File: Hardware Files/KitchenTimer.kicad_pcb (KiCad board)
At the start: 2 copper layers, 100 x 100 mm, 89 parts, among them J1 Conn_01x04, J2 USB_B_Micro, J3 Battery, Q1 P 1V 250uA 4A SOT-23, Q10 Q_NMOS_GSD, Q11 Q_NMOS_GSD, Q12 Q_NMOS_GSD, Q13 Q_NMOS_GSD, Q14 -30V 12A 14mΩ @ 8A, Q15 20V 7.5A 24mΩ @ 2.5Vgs, Q2 P 1V 250uA 4A SOT-23, Q3 P 1V 250uA 4A SOT-23, Q4 P 1V 250uA 4A SOT-23, Q5 P 1V 250uA 4A SOT-23, Q6 Q_NMOS_GSD, Q7 Q_NMOS_GSD, Q8 Q_NMOS_GSD, Q9 Q_NMOS_GSD, SW1 SW_SPST, SW2 SW_SPST, SW3 SW_Push_Dual, SW4 SW_Push_Dual, SW5 SW_Push_Dual, SW6 SW_Push_Dual, U1 74HC595, U2 74HC595, U3 ESP-WROOM-02D, U4 AP34063S8G-13, U5 TP4056, U6 AP9101CK6, U7 NCP1117ST50T3G, U8 NCP1117ST33T3G

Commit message: update layout
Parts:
- added C1: 1uF, Capacitor_SMD:C_1206_3216Metric_Pad1.33x1.80mm_HandSolder, B.Cu at (162.0, -12.0)
- added C10: 1uF, Capacitor_SMD:C_1206_3216Metric_Pad1.33x1.80mm_HandSolder, B.Cu at (152.4, -15.3)
- added C2: 1uF, Capacitor_SMD:C_1206_3216Metric_Pad1.33x1.80mm_HandSolder, B.Cu at (162.0, -15.3)
- added C3: 1uF, Capacitor_SMD:C_1206_3216Metric_Pad1.33x1.80mm_HandSolder, B.Cu at (40.0, -21.5)
- added C4: 10uF, Capacitor_SMD:C_1206_3216Metric_Pad1.33x1.80mm_HandSolder, B.Cu at (42.5, -21.5)
- added C5: 1uF, Capacitor_SMD:C_1206_3216Metric_Pad1.33x1.80mm_HandSolder, B.Cu at (146.4, -12.0)
- added C6: 1uF, Capacitor_SMD:C_1206_3216Metric_Pad1.33x1.80mm_HandSolder, B.Cu at (140.4, -18.7)
- added C7: 1uF, Capacitor_SMD:C_1206_3216Metric_Pad1.33x1.80mm_HandSolder, B.Cu at (146.4, -15.3)
- added C8: 1uF, Capacitor_SMD:C_1206_3216Metric_Pad1.33x1.80mm_HandSolder, B.Cu at (152.4, -12.0)
- added C9: 1uF, Capacitor_SMD:C_1206_3216Metric_Pad1.33x1.80mm_HandSolder, B.Cu at (146.4, -18.7)
- moved R23 190.7 mm to (28.0, 46.0), turned to 90 degrees
- moved R24 190.4 mm to (28.0, 54.0), turned to 90 degrees
- moved Q11 187.7 mm to (31.0, 50.0), turned to 0 degrees
- moved Q6 184.7 mm to (31.0, 46.0), turned to 0 degrees
- moved Q7 184.5 mm to (31.0, 54.0), turned to 0 degrees
- moved R27 176.0 mm to (42.5, 69.0), turned to 180 degrees
- moved U3 174.1 mm to (37.0, -19.5)
- moved Q10 173.2 mm to (42.5, 66.0), turned to 90 degrees
- moved R26 171.7 mm to (46.5, 69.0), turned to 180 degrees
- moved Q9 168.9 mm to (46.5, 66.0), turned to 90 degrees
- moved Q13 167.4 mm to (50.5, 66.0), turned to 90 degrees
- moved R25 163.5 mm to (54.5, 69.0), turned to 180 degrees
- moved Q8 160.6 mm to (54.5, 66.0), turned to 90 degrees
- moved Q12 158.6 mm to (58.5, 66.0), turned to 90 degrees
- moved R18 154.4 mm to (40.0, 35.0), turned to 180 degrees
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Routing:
- net Net-(LED1-Pad9): track 0.00 -> 25.3 mm
- net Net-(LED1-Pad12): track 0.00 -> 15.6 mm
- net Net-(LED1-Pad13): track 0.00 -> 11.7 mm
- net LED_G_Sink: track 0.00 -> 6.83 mm
- net LED_C_Sink: track 0.00 -> 6.50 mm
- net LED_DP_Sink: track 0.00 -> 5.00 mm
- net LED_B_Sink: track 0.00 -> 4.71 mm
- net LED_D_Sink: track 0.00 -> 3.50 mm
- net Net-(LED1-Pad1): track 0.00 -> 3.43 mm
- net Net-(LED1-Pad2): track 0.00 -> 3.41 mm
- net Net-(LED1-Pad5): track 0.00 -> 3.40 mm
- net Net-(LED1-Pad3): track 0.00 -> 3.40 mm
- net Net-(LED1-Pad4): track 0.00 -> 3.38 mm
- net LED_F_Sink: track 0.00 -> 3.21 mm
- net Char_3: track 0.00 -> 2.05 mm
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
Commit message: reorganize mosfets
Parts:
- removed Q5: P 1V 250uA 4A SOT-23, Package_TO_SOT_SMD:SOT-23
- removed R22: 10k, Resistor_SMD:R_0805_2012Metric_Pad1.20x1.40mm_HandSolder
- moved C2 173.1 mm to (-7.00, 22.0), turned to 90 degrees
- moved C1 157.7 mm to (8.00, 22.0), turned to 90 degrees
- moved R14 130.1 mm to (-72.0, 32.0)
- moved R15 130.1 mm to (-56.0, 31.5)
- moved R29 87.1 mm to (-24.0, 41.0), turned to 0 degrees
- moved Q12 85.1 mm to (-24.0, 45.0), turned to 270 degrees
- moved R12 77.4 mm to (-24.0, 50.0), turned to 90 degrees
- moved R30 75.6 mm to (-24.0, 56.0), turned to 0 degrees
- moved Q13 74.7 mm to (-24.0, 60.0), turned to 270 degrees
- moved R13 71.6 mm to (-24.0, 65.0), turned to 90 degrees
- moved R26 67.6 mm to (-15.0, 41.0), turned to 0 degrees
- moved Q9 65.0 mm to (-15.0, 45.0), turned to 270 degrees
- moved Q8 62.2 mm to (-7.00, 75.0), turned to 270 degrees
- moved R25 61.5 mm to (-7.00, 71.0), turned to 0 degrees
- moved R21 61.4 mm to (-1.00, 41.0), turned to 180 degrees
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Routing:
- net LED_C: track 0.00 -> 61.6 mm
- net LED_F: track 0.00 -> 58.4 mm
- net Char_1: track 2.05 -> 57.1 mm
- net LED_E: track 0.00 -> 49.3 mm
- net LED_B: track 0.00 -> 45.5 mm
- net LED_DP: track 0.00 -> 44.8 mm
- net Char_2: track 2.05 -> 40.6 mm
- net LED_D: track 0.00 -> 36.7 mm
- net Char_3: track 2.05 -> 30.8 mm
- net LED_G: track 2.02 -> 28.2 mm
- net Net-(LED1-Pad9): track 25.3 -> 0.00 mm
- net LED_A: track 0.00 -> 23.5 mm
- net Char_4: track 0.00 -> 21.4 mm
- net Net-(LED1-Pad12): track 15.6 -> 0.00 mm
- net Net-(LED1-Pad13): track 11.7 -> 0.00 mm
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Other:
- board size 100 x 100 mm -> 200 x 100 mm

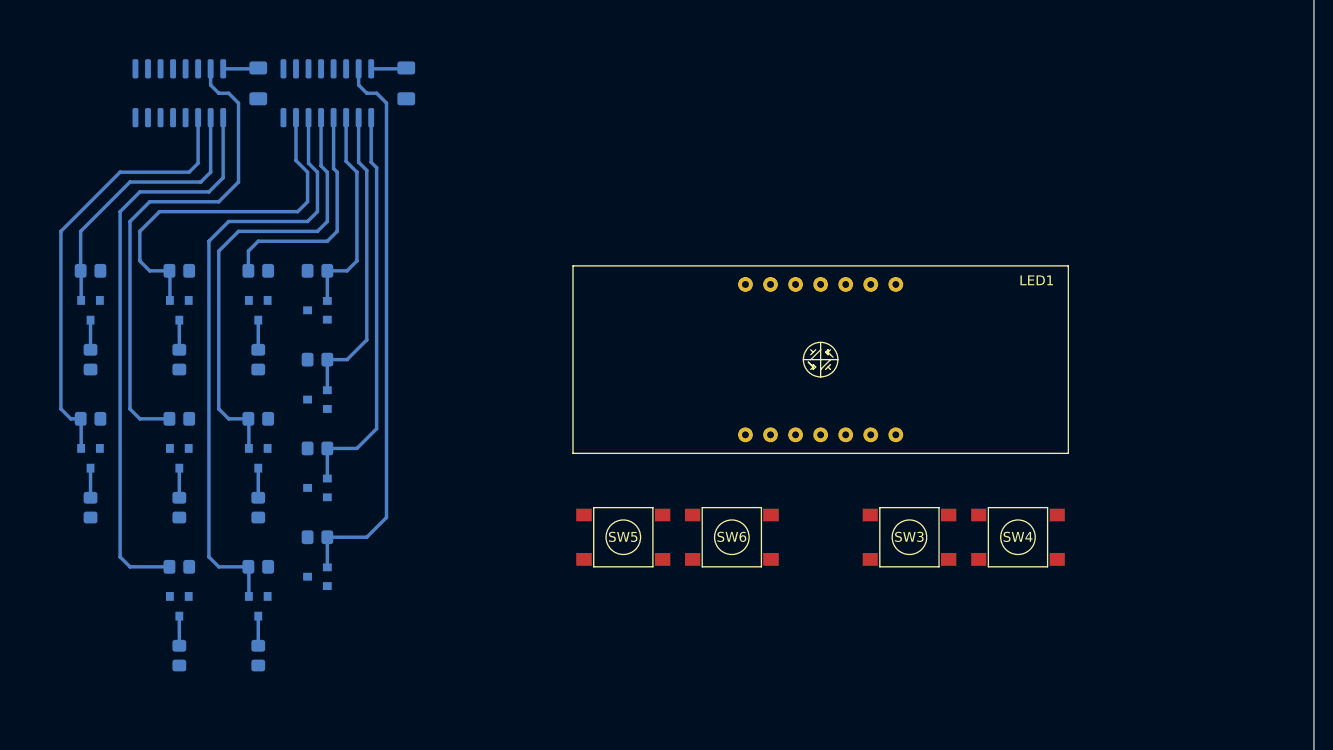
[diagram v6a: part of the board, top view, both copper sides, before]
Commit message: layout mosfets
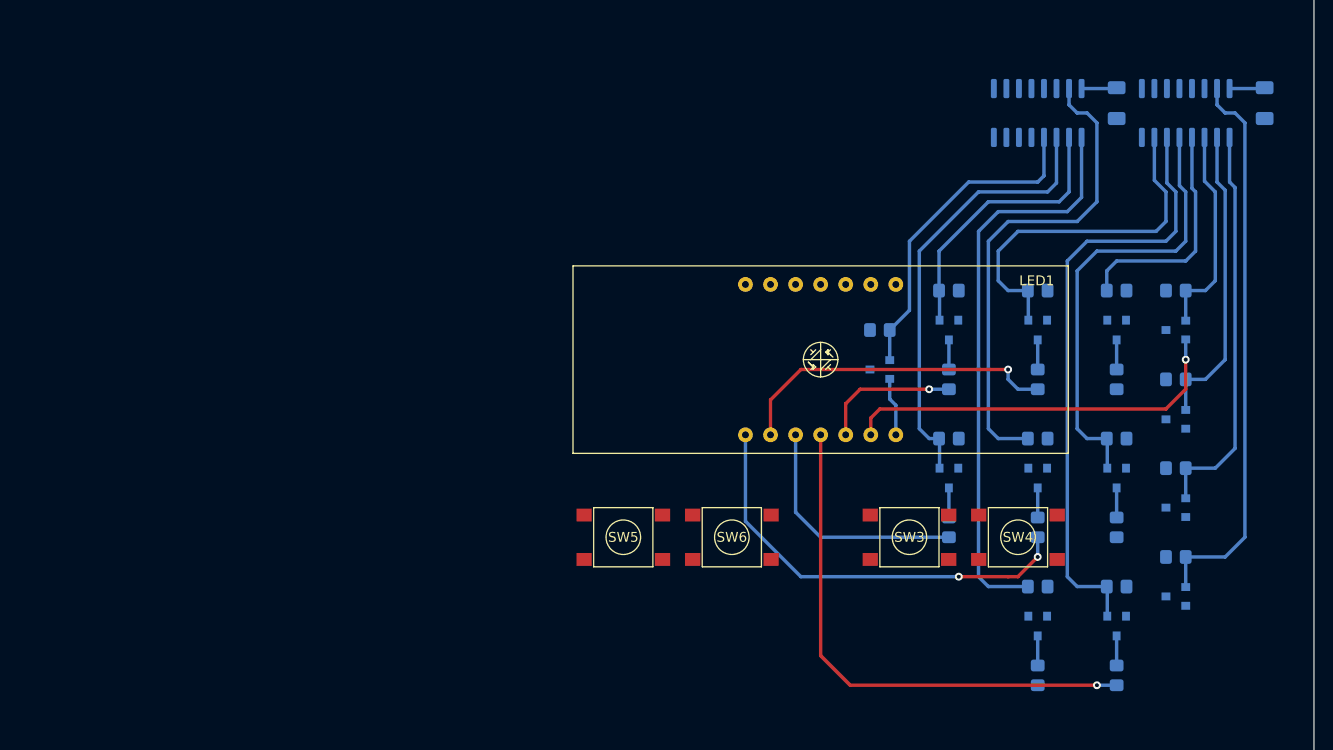
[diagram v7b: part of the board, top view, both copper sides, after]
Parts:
- added Q5: P 1V 250uA 4A SOT-23, Package_TO_SOT_SMD:SOT-23, B.Cu at (56.0, 51.0)
- added R22: 10k, Resistor_SMD:R_0805_2012Metric_Pad1.20x1.40mm_HandSolder, B.Cu at (56.0, 47.0)
- moved C1 87.0 mm to (95.0, 24.0)
- moved C2 87.0 mm to (80.0, 24.0)
- moved Q1 87.0 mm to (86.0, 74.0)
- moved Q10 87.0 mm to (72.0, 62.0)
- moved Q11 87.0 mm to (72.0, 77.0)
- moved Q12 87.0 mm to (63.0, 47.0)
- moved Q13 87.0 mm to (63.0, 62.0)
- moved Q2 87.0 mm to (86.0, 65.0)
- moved Q3 87.0 mm to (86.0, 56.0)
- moved Q4 87.0 mm to (86.0, 47.0)
- moved Q6 87.0 mm to (80.0, 47.0)
- moved Q7 87.0 mm to (80.0, 62.0)
- moved Q8 87.0 mm to (80.0, 77.0)
- moved Q9 87.0 mm to (72.0, 47.0)
- moved R10 87.0 mm to (72.0, 67.0)
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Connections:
- U2 pad 4: Unused_QE -> LED_(':')
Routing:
- net Net-(LED1-Pad4): track 0.00 -> 53.6 mm, vias 0 -> 1
- net Net-(LED1-Pad1): track 0.00 -> 43.5 mm, vias 0 -> 2
- net Char_4_Power: track 0.00 -> 39.9 mm, vias 0 -> 1
- net Net-(LED1-Pad2): track 0.00 -> 33.3 mm, vias 0 -> 1
- net LED_(':'): track 0.00 -> 33.2 mm
- net Net-(LED1-Pad3): track 0.00 -> 24.4 mm
- net Net-(LED1-Pad5): track 0.00 -> 14.2 mm, vias 0 -> 1
- net Char_(':')_Power: track 0.00 -> 5.93 mm

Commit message: change architecture approach
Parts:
- added LED2: SLR0564DBA4BD, KitchenTimer:SLR0564DBA4BD, F.Cu at (193.0, -76.2)
- added Q16: P 1V 250uA 4A SOT-23, Package_TO_SOT_SMD:SOT-23, B.Cu at (179.8, -83.3)
- added Q17: P 1V 250uA 4A SOT-23, Package_TO_SOT_SMD:SOT-23, B.Cu at (179.8, -79.8)
- added Q18: P 1V 250uA 4A SOT-23, Package_TO_SOT_SMD:SOT-23, B.Cu at (179.8, -76.2)
- added Q19: P 1V 250uA 4A SOT-23, Package_TO_SOT_SMD:SOT-23, B.Cu at (179.8, -69.1)
- added Q20: P 1V 250uA 4A SOT-23, Package_TO_SOT_SMD:SOT-23, B.Cu at (179.8, -72.6)
- added R1: R, Resistor_SMD:R_0603_1608Metric_Pad0.98x0.95mm_HandSolder, B.Cu at (203.7, -78.7)
- added R2: R, Resistor_SMD:R_0603_1608Metric_Pad0.98x0.95mm_HandSolder, B.Cu at (203.7, -81.8)
- added R3: R, Resistor_SMD:R_0603_1608Metric_Pad0.98x0.95mm_HandSolder, B.Cu at (203.7, -72.6)
- added R4: R, Resistor_SMD:R_0603_1608Metric_Pad0.98x0.95mm_HandSolder, B.Cu at (203.7, -75.7)
- added R46: R, Resistor_SMD:R_0603_1608Metric_Pad0.98x0.95mm_HandSolder, B.Cu at (203.7, -80.3)
- added R47: R, Resistor_SMD:R_0603_1608Metric_Pad0.98x0.95mm_HandSolder, B.Cu at (203.7, -71.1)
- added R48: R, Resistor_SMD:R_0603_1608Metric_Pad0.98x0.95mm_HandSolder, B.Cu at (203.7, -74.2)
- added R49: 10k, Resistor_SMD:R_0603_1608Metric_Pad0.98x0.95mm_HandSolder, B.Cu at (176.8, -83.3)
- added R5: R, Resistor_SMD:R_0603_1608Metric_Pad0.98x0.95mm_HandSolder, B.Cu at (203.7, -77.2)
- added R50: 10k, Resistor_SMD:R_0603_1608Metric_Pad0.98x0.95mm_HandSolder, B.Cu at (176.8, -79.8)
- added R51: 10k, Resistor_SMD:R_0603_1608Metric_Pad0.98x0.95mm_HandSolder, B.Cu at (176.8, -76.2)
- added R52: 10k, Resistor_SMD:R_0603_1608Metric_Pad0.98x0.95mm_HandSolder, B.Cu at (176.8, -69.1)
- added R53: 10k, Resistor_SMD:R_0603_1608Metric_Pad0.98x0.95mm_HandSolder, B.Cu at (176.8, -72.6)
- added U11: 74HC595, Package_SO:SOIC-16_3.9x9.9mm_P1.27mm, B.Cu at (170.2, -86.9)
- added U9: 74HC595, Package_SO:SOIC-16_3.9x9.9mm_P1.27mm, B.Cu at (210.8, -86.9)
- R18, R19, R20, R21, R22: footprint Resistor_SMD:R_0805_2012Metric_Pad1.20x1.40mm_HandSolder -> Resistor_SMD:R_0603_1608Metric_Pad0.98x0.95mm_HandSolder
- U3: moved to F.Cu
- moved R15 181.1 mm to (124.0, 11.5)
- moved J1 157.6 mm to (28.6, 4.00)
- moved R14 128.1 mm to (56.0, 37.0)
- moved R17 107.9 mm to (74.0, 17.0), turned to 270 degrees
- moved J2 77.4 mm to (186.9, 20.3)
- moved R31 61.2 mm to (204.9, 37.3)
- moved R32 61.2 mm to (208.2, 37.3)
- moved R36 61.2 mm to (201.4, 62.6)
- moved C10 61.2 mm to (188.0, 34.4)
- moved C5 61.2 mm to (181.9, 37.8)
- moved C6 61.2 mm to (175.9, 31.1)
- moved C7 61.2 mm to (181.9, 34.4)
- moved C8 61.2 mm to (188.0, 37.8)
- moved C9 61.2 mm to (181.9, 31.1)
- moved R33 61.2 mm to (202.1, 43.3)
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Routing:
- net Char_1_Power: track 0.00 -> 99.5 mm
- net Char_2_Power: track 0.00 -> 74.8 mm, vias 0 -> 4
- net Net-(LED1-Pad12): track 0.00 -> 73.9 mm, vias 0 -> 1
- net Latch: track 0.00 -> 71.4 mm, vias 0 -> 3
- net Char_3_Power: track 0.00 -> 69.8 mm, vias 0 -> 2
- net Data: track 0.00 -> 69.2 mm, vias 0 -> 2
- net Net-(LED1-Pad9): track 0.00 -> 67.7 mm, vias 0 -> 1
- net Clock: track 0.00 -> 61.7 mm, vias 0 -> 3
- net !Clear: track 0.00 -> 48.4 mm
- net Net-(LED1-Pad13): track 0.00 -> 47.5 mm, vias 0 -> 1
- net LED_G: track 28.2 -> 60.2 mm
- net Net-(LED2-Pad1): track 0.00 -> 25.1 mm
- net Char_(':')_Power: track 5.93 -> 29.7 mm, vias 0 -> 1
- net Char_4: track 21.4 -> 44.5 mm
- net ESP_RX: track 0.00 -> 22.8 mm
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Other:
- board size 200 x 100 mm -> 100 x 100 mm
